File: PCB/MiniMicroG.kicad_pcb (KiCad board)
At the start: 2 copper layers, 111.9 x 88.1 mm, 21 parts, among them J1 .91"OLED, SW1 CHERRY_MX, SW2 CHERRY_MX, SW4 CHERRY_MX, SW5 CHERRY_MX, SW6 CHERRY_MX, SW7 RotaryEncoder_Switch, SW8 CHERRY_MX, U1 XIAO-RP2040-DIP

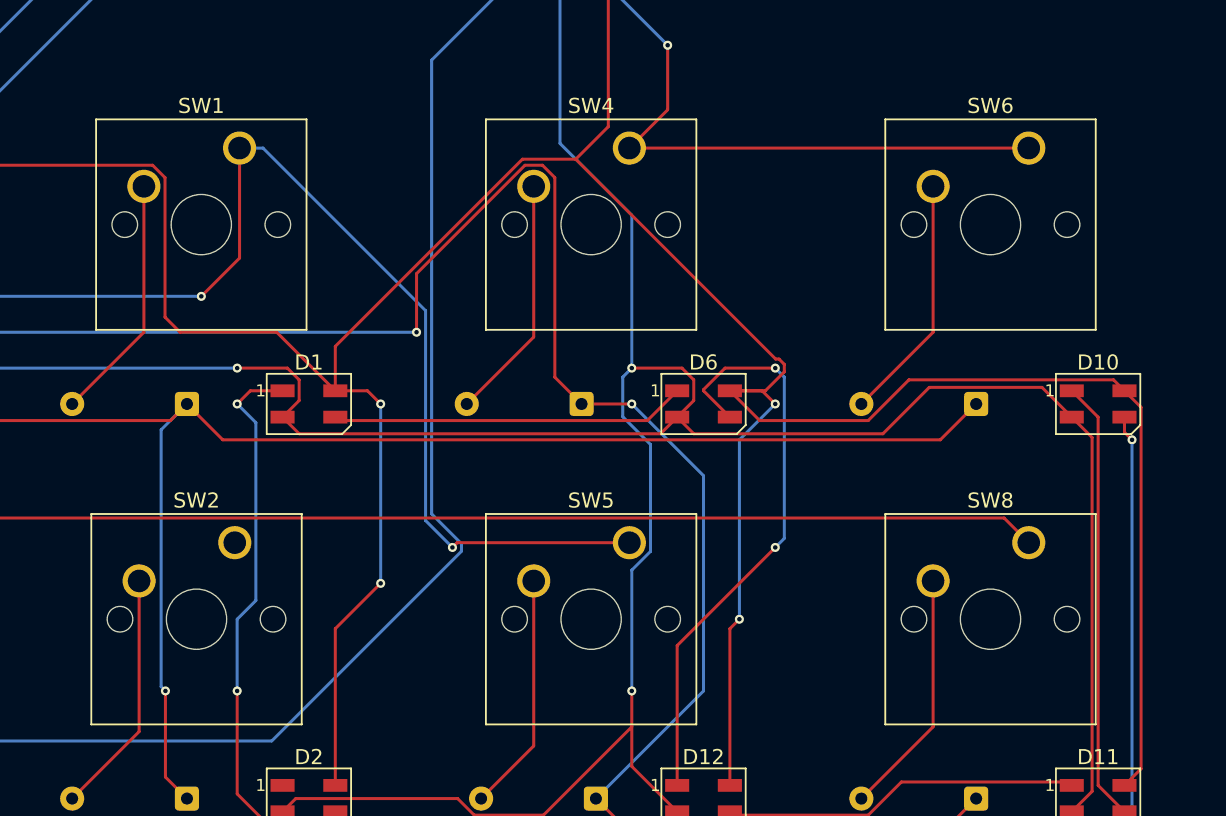
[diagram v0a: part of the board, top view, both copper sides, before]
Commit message: Add 3D Models
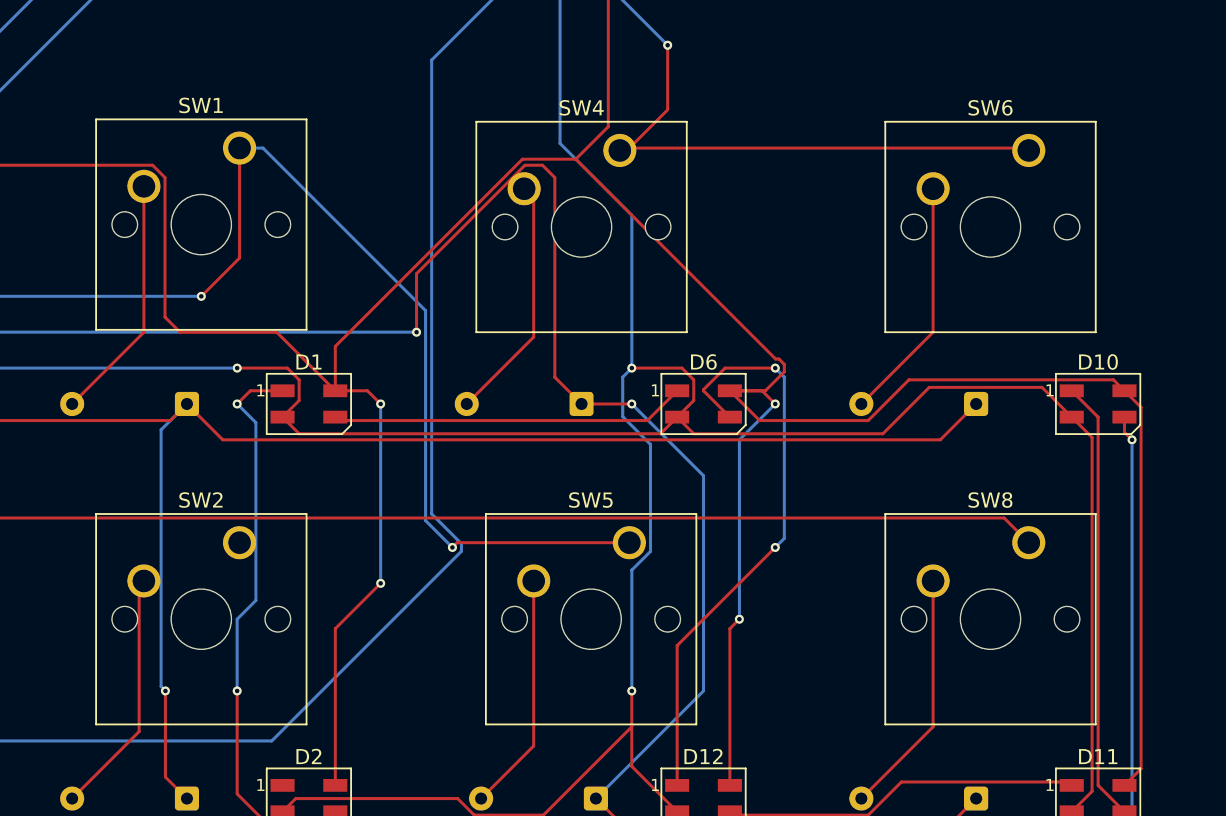
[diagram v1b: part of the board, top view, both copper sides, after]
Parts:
- moved SW4 0.65 mm to (149.2, 78.4)
- moved SW2 0.32 mm to (124.0, 104.5)
- moved SW6 0.16 mm to (176.4, 78.4)
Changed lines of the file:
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@@
 			)
 		)
+		(model "${KIPRJMOD}/3D Models/EVQV9_RotaryEncoder.step"
+			(offset
+				(xyz 7.5 -2 0)
+			)
+			(scale
+				(xyz 1 1 1)
+			)
+			(rotate
+				(xyz -0 -0 90)
+			)
+		)
 	)
 	(footprint "LED_SMD:LED_SK6812MINI_PLCC4_3.5x3.5mm_P1.75mm"
@@
 			)
 		)
+		(model "${KIPRJMOD}/3D Models/LED_SK6812MINI-E.step"
+			(offset
+				(xyz 0 5 -1)
+			)
+			(scale
+				(xyz 1 1 1)
+			)
+			(rotate
+				(xyz -0 -180 -0)
+			)
+		)
 	)
 	(footprint "Button_Switch_Keyboard:SW_Cherry_MX_1.00u_PCB"
@@
 			)
 		)
+		(model "${KIPRJMOD}/3D Models/cherry-mx-1.snapshot.3/asm_mx_asm_PCB.stp"
+			(offset
+				(xyz -2 -5 4)
+			)
+			(scale
+				(xyz 1 1 1)
+			)
+			(rotate
+				(xyz -0 -180 -90)
+			)
+		)
 	)
 	(footprint "Button_Switch_Keyboard:SW_Cherry_MX_1.00u_PCB"
@@
 		(model "${KICAD9_3DMODEL_DIR}/Button_Switch_Keyboard.3dshapes/SW_Cherry_MX_1.00u_PCB.step"
 			(offset
-				(xyz 0 0 0)
+				(xyz 2.1 0 0)
 			)
 			(scale
@@
 			)
 			(rotate
-				(xyz 0 0 0)
+				(xyz -0 -0 -0)
+			)
+		)
+		(model "${KIPRJMOD}/3D Models/cherry-mx-1.snapshot.3/asm_mx_asm_PCB.stp"
+			(offset
+				(xyz -2 -5 4)
+			)
+			(scale
+				(xyz 1 1 1)
+			)
+			(rotate
+				(xyz -0 -180 -90)
 			)
 		)
@@
 			)
 		)
+		(model "${KIPRJMOD}/3D Models/LED_SK6812MINI-E.step"
+			(offset
+				(xyz 0 5 -1)
+			)
+			(scale
+				(xyz 1 1 1)
+			)
+			(rotate
+				(xyz -0 -180 -0)
+			)
+		)
 	)
 	(footprint "LED_SMD:LED_SK6812MINI_PLCC4_3.5x3.5mm_P1.75mm"
@@
 			)
 		)
+		(model "${KIPRJMOD}/3D Models/LED_SK6812MINI-E.step"
+			(offset
+				(xyz 0 5 -1)
+			)
+			(scale
+				(xyz 1 1 1)
+			)
+			(rotate
+				(xyz -0 -180 -0)
+			)
+		)
 	)
 	(footprint "Seeed Studio XIAO Series Library:XIAO-RP2040-DIP"
@@
 			)
 		)
+		(model "${KIPRJMOD}/3D Models/Seeed Studio XIAO RP2040 v26.step"
+			(offset
+				(xyz 0 0 0)
+			)
+			(scale
+				(xyz 1 1 1)
+			)
+			(rotate
+				(xyz 0 0 0)
+			)
+		)
 	)
 	(footprint "Button_Switch_Keyboard:SW_Cherry_MX_1.00u_PCB"
 		(layer "F.Cu")
-		(at 123.66625 104.4575)
+		(at 123.98375 104.4575)
 		(descr "Cherry MX keyswitch, 1.00u, PCB mount, http://cherryamericas.com/wp-content/uploads/2014/12/mx_cat.pdf")
 		(tags "Cherry MX keyswitch 1.00u PCB")
@@
 			)
 		)
+		(model "${KIPRJMOD}/3D Models/cherry-mx-1.snapshot.3/asm_mx_asm_PCB.stp"
+			(offset
+				(xyz -2 -5 4)
+			)
+			(scale
+				(xyz 1 1 1)
+			)
+			(rotate
+				(xyz -0 -180 -90)
+			)
+		)
 	)
 	(footprint "KiCad-4_pin-SSD1306_OLED-.91-128x32:SSD1306-0.91-OLED-4pin-128x32"
@@
 		)
 		(embedded_fonts no)
+		(model "${KIPRJMOD}/3D Models/OLED_0.91_128x32.stp"
+			(offset
+				(xyz 19 -6 0)
+			)
+			(scale
+				(xyz 1 1 1)
+			)
+			(rotate
+				(xyz -0 -0 -180)
+			)
+		)
 	)
 	(footprint "LED_SMD:LED_SK6812MINI_PLCC4_3.5x3.5mm_P1.75mm"
@@
 			)
 		)
+		(model "${KIPRJMOD}/3D Models/LED_SK6812MINI-E.step"
+			(offset
+				(xyz 0 5 -1)
+			)
+			(scale
+				(xyz 1 1 1)
+			)
+			(rotate
+				(xyz -0 -180 -0)
+			)
+		)
 	)
 	(footprint "LED_SMD:LED_SK6812MINI_PLCC4_3.5x3.5mm_P1.75mm"
@@
 			)
 		)
+		(model "${KIPRJMOD}/3D Models/LED_SK6812MINI-E.step"
+			(offset
+				(xyz 0 5 -1)
+			)
+			(scale
+				(xyz 1 1 1)
+			)
+			(rotate
+				(xyz -0 -180 -0)
+			)
+		)
 	)
 	(footprint "Button_Switch_Keyboard:SW_Cherry_MX_1.00u_PCB"
 		(layer "F.Cu")
-		(at 149.86 78.26375)
+		(at 149.225 78.4225)
 		(descr "Cherry MX keyswitch, 1.00u, PCB mount, http://cherryamericas.com/wp-content/uploads/2014/12/mx_cat.pdf")
 		(tags "Cherry MX keyswitch 1.00u PCB")
@@
 			)
 		)
+		(model "${KIPRJMOD}/3D Models/cherry-mx-1.snapshot.3/asm_mx_asm_PCB.stp"
+			(offset
+				(xyz -2 -5 5)
+			)
+			(scale
+				(xyz 1 1 1)
+			)
+			(rotate
+				(xyz -0 180 -90)
+			)
+		)
 	)
 	(footprint "LED_SMD:LED_SK6812MINI_PLCC4_3.5x3.5mm_P1.75mm"
@@
 			)
 		)
+		(model "${KIPRJMOD}/3D Models/LED_SK6812MINI-E.step"
+			(offset
+				(xyz 0 5 -1)
+			)
+			(scale
+				(xyz 1 1 1)
+			)
+			(rotate
+				(xyz -0 -180 -0)
+			)
+		)
 	)
 	(footprint "Button_Switch_Keyboard:SW_Cherry_MX_1.00u_PCB"
@@
 			)
 		)
+		(model "${KIPRJMOD}/3D Models/cherry-mx-1.snapshot.3/asm_mx_asm_PCB.stp"
+			(offset
+				(xyz -2 -5 4)
+			)
+			(scale
+				(xyz 1 1 1)
+			)
+			(rotate
+				(xyz -0 -180 -90)
+			)
+		)
 	)
 	(footprint "Button_Switch_Keyboard:SW_Cherry_MX_1.00u_PCB"
 		(layer "F.Cu")
-		(at 176.37125 78.26375)
+		(at 176.37125 78.4225)
 		(descr "Cherry MX keyswitch, 1.00u, PCB mount, http://cherryamericas.com/wp-content/uploads/2014/12/mx_cat.pdf")
 		(tags "Cherry MX keyswitch 1.00u PCB")
@@
 		(embedded_fonts no)
 		(model "${KICAD9_3DMODEL_DIR}/Button_Switch_Keyboard.3dshapes/SW_Cherry_MX_1.00u_PCB.step"
+			(hide yes)
 			(offset
 				(xyz 0 0 0)
@@
 			)
 		)
+		(model "${KIPRJMOD}/3D Models/asm_mx.asm.16"
+			(hide yes)
+			(offset
+				(xyz 0 0 0)
+			)
+			(scale
+				(xyz 1 1 1)
+			)
+			(rotate
+				(xyz 0 0 0)
+			)
+		)
+		(model "${KIPRJMOD}/3D Models/cherry-mx-1.snapshot.3/asm_mx_asm_PCB.stp"
+			(offset
+				(xyz -2.5 -5 5)
+			)
+			(scale
+				(xyz 1 1 1)
+			)
+			(rotate
+				(xyz -0 -180 -90)
+			)
+		)
+		(model "${KIPRJMOD}/3D Models/cherry-mx-1.snapshot.3/asm_mx_asm_PLATE.stp"
+			(hide yes)
+			(offset
+				(xyz 2 0 0)
+			)
+			(scale
+				(xyz 1 1 1)
+			)
+			(rotate
+				(xyz -0 -0 -0)
+			)
+		)
 	)
 	(footprint "Diode_THT:D_DO-35_SOD27_P7.62mm_Horizontal"
@@
 		(width 0.2)
 		(layer "B.Cu")
-		(net 26)
-	)
-	(segment
-		(start 183.226 97.63125)
-		(end 183.35625 97.63125)
-		(width 0.2)
-		(layer "B.Cu")

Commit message: Update PCB
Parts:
- moved D9 25.3 mm to (149.0, 113.0), turned to 90 degrees
- moved D3 23.9 mm to (149.0, 94.8), turned to 90 degrees
- moved D10 23.4 mm to (158.0, 99.5)
- moved D11 23.1 mm to (158.0, 119.0), turned to 180 degrees
- moved D8 19.6 mm to (130.0, 113.0), turned to 90 degrees
- moved J1 18.5 mm to (168.9, 75.9)
- moved SW6 17.1 mm to (160.7, 85.1)
- moved D7 16.7 mm to (130.0, 95.0), turned to 90 degrees
- moved D6 16.4 mm to (139.0, 99.5)
- moved D12 15.7 mm to (139.2, 119.0), turned to 180 degrees
- moved SW8 15.7 mm to (160.7, 104.1)
- moved D5 13.5 mm to (110.0, 113.0), turned to 90 degrees
- moved SW7 10.6 mm to (108.0, 65.0)
- moved D4 10.5 mm to (110.0, 95.0), turned to 90 degrees
- moved D1 10.3 mm to (119.2, 99.5)
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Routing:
- net GND: track 267.0 -> 31.1 mm, vias 4 -> 7
- net +5V: track 252.8 -> 184.7 mm, vias 4 -> 0
- net Net-(U1-GPIO28/ADC2/A2): track 0.00 -> 63.6 mm
- net Net-(U1-GPIO27/ADC1/A1): track 0.00 -> 58.3 mm
- net Net-(D7-K): track 140.4 -> 82.2 mm
- net Net-(D3-K): track 114.6 -> 65.1 mm, vias 1 -> 0
- net Net-(D10-DIN): track 131.9 -> 105.0 mm, vias 1 -> 0
- net Net-(U1-GPIO1/RX): track 89.2 -> 63.3 mm, vias 3 -> 0
- net Net-(U1-GPIO0/TX): track 133.1 -> 108.4 mm, vias 1 -> 0
- net Net-(J1-Pin_3): track 124.6 -> 102.2 mm
- net Net-(U1-GPIO29/ADC3/A3): track 91.3 -> 109.9 mm, vias 1 -> 0
- net Net-(J1-Pin_4): track 105.5 -> 87.8 mm
- net Net-(D1-DOUT): track 37.9 -> 23.2 mm, vias 2 -> 0
- net Net-(U1-GPIO2/SCK): track 81.2 -> 69.3 mm
- net Net-(D3-A): track 16.4 -> 5.49 mm
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- added copper zone on B.Cu, net GND
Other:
- board size 111.9 x 88.1 mm -> 98 x 75 mm

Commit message: Update PCB
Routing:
- net GND: track 31.1 -> 70.7 mm
- net Net-(U1-GPIO29/ADC3/A3): track 109.9 -> 89.7 mm, vias 0 -> 3
- net Net-(D3-K): track 65.1 -> 84.1 mm
- net Net-(U1-GPIO28/ADC2/A2): track 63.6 -> 68.7 mm, vias 0 -> 2
- net +5V: track 184.7 -> 186.9 mm, vias 0 -> 2
- net Net-(J1-Pin_3): track 102.2 -> 103.1 mm

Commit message: Made the Casing
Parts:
- moved J1 3.16 mm to (167.9, 72.9)
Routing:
- net Net-(J1-Pin_3): track 103.1 -> 96.9 mm
- net +5V: track 186.9 -> 189.8 mm
- net Net-(J1-Pin_4): track 87.8 -> 88.0 mm, vias 0 -> 1
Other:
- board text added: "SCL"
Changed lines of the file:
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@@
 		(embedded_fonts no)
 		(model "${KICAD9_3DMODEL_DIR}/Rotary_Encoder.3dshapes/RotaryEncoder_Alps_EC11E-Switch_Vertical_H20mm.step"
+			(hide yes)
 			(offset
 				(xyz 0 0 0)
@@
 		)
 		(model "${KIPRJMOD}/3D Models/EVQV9_RotaryEncoder.step"
+			(hide yes)
 			(offset
 				(xyz 7.5 -2 0)
@@
 			)
 		)
+		(model "${KIPRJMOD}/3D Models/ec11.STEP"
+			(offset
+				(xyz 7.5 -2.5 0)
+			)
+			(scale
+				(xyz 1 1 1)
+			)
+			(rotate
+				(xyz -90 -0 -90)
+			)
+		)
+		(model "${KIPRJMOD}/3D Models/EC11-THT-15F-black.step"
+			(hide yes)
+			(offset
+				(xyz 7.5 -2.5 0)
+			)
+			(scale
+				(xyz 1 1 1)
+			)
+			(rotate
+				(xyz -0 -0 90)
+			)
+		)
 	)
 	(footprint "LED_SMD:LED_SK6812MINI_PLCC4_3.5x3.5mm_P1.75mm"
@@
 	(footprint "KiCad-4_pin-SSD1306_OLED-.91-128x32:SSD1306-0.91-OLED-4pin-128x32"
 		(layer "F.Cu")
-		(at 168.885 75.885 180)
+		(at 167.885 72.885 180)
 		(property "Reference" "J1"
 			(at 1.9 5.91 90)
@@
 			)
 		)
-		(fp_text user "SCL"
-			(at 34.5 7.27 90)
-			(layer "F.SilkS")
-			(effects
-				(font
-					(size 0.75 0.75)
-					(thickness 0.15)
-				)
-			)
-		)
 		(pad "1" thru_hole rect
 			(at 36.5 2.19 180)
@@
 		)
 	)
+	(gr_text "SCL"
+		(at 133.385 65.615 90)
+		(layer "F.SilkS")
+		(effects
+			(font
+				(size 0.75 0.75)
+				(thickness 0.15)
+			)
+		)
+	)
 	(gr_text "Created by @codecooker1"
 		(at 104 55 -0)
@@
 	)
 	(segment
-		(start 135 80.538274)
-		(end 135 72.885)
-		(width 0.3)
-		(layer "F.Cu")
-		(net 3)
-	)
-	(segment
 		(start 137.5 119.875)
 		(end 136.724 120.651)
@@
 	)
 	(segment
-		(start 143.546 86.546)
-		(end 141.007726 86.546)
-		(width 0.3)
-		(layer "F.Cu")
-		(net 3)
-	)
-	(segment
 		(start 120.224 97.899)
 		(end 111.101 97.899)
@@
 	)
 	(segment
-		(start 133.27 71.155)
-		(end 132.385 71.155)
-		(width 0.3)
-		(layer "F.Cu")
-		(net 3)
-	)
-	(segment
 		(start 136.724 120.651)
 		(end 118.276 120.651)
@@
 	)
 	(segment
-		(start 141.007726 86.546)
-		(end 135 80.538274)
-		(width 0.3)
-		(layer "F.Cu")
-		(net 3)
-	)
-	(segment
 		(start 158.974 97.899)
 		(end 159.75 98.675)
@@
 	)
 	(segment
+		(start 135 80.538274)
+		(end 135 71.77)
+		(width 0.3)
+		(layer "F.Cu")
+		(net 3)
+	)
+	(segment
 		(start 152 97.899)
 		(end 158.974 97.899)
@@
 	)
 	(segment
+		(start 152 97.899)
+		(end 152 95)
+		(width 0.3)
+		(layer "F.Cu")
+		(net 3)
+	)
+	(segment
 		(start 156.25 119.875)
 		(end 155.474 120.651)
@@
 	)
 	(segment
-		(start 152 95)
-		(end 143.546 86.546)
+		(start 135 71.77)
+		(end 131.385 68.155)
 		(width 0.3)
 		(layer "F.Cu")
@@
 	)
 	(segment
-		(start 152 97.899)
-		(end 152 95)
+		(start 106.349 97.651)
+		(end 85.53137 97.651)
 		(width 0.3)
 		(layer "F.Cu")
@@
 	)
 	(segment
-		(start 106.349 97.651)
-		(end 85.53137 97.651)
+		(start 108 96)
+		(end 106.349 97.651)
 		(width 0.3)
 		(layer "F.Cu")
@@
 	)
 	(segment
-		(start 108 96)
-		(end 106.349 97.651)
+		(start 143.546 86.546)
+		(end 141.007726 86.546)
 		(width 0.3)
 		(layer "F.Cu")
@@
 	)
 	(segment
-		(start 135 72.885)
-		(end 133.27 71.155)
+		(start 152 95)
+		(end 143.546 86.546)
+		(width 0.3)
+		(layer "F.Cu")
+		(net 3)
+	)
+	(segment
+		(start 141.007726 86.546)
+		(end 135 80.538274)
 		(width 0.3)
 		(layer "F.Cu")
@@
 	)
 	(segment
+		(start 126.649 66.351)
+		(end 127 66)
+		(width 0.3)
+		(layer "F.Cu")
+		(net 6)
+	)
+	(segment
 		(start 114.684662 66.351)
-		(end 132.109 66.351)
+		(end 126.649 66.351)
 		(width 0.3)
 		(layer "F.Cu")
@@
 	)
 	(segment
-		(start 132.109 66.351)
-		(end 132.385 66.075)
+		(start 92.04 117.62)
+		(end 80.767 106.347)
 		(width 0.3)
 		(layer "F.Cu")
 		(net 6)
 	)
+	(via
+		(at 127 66)
+		(size 0.6)
+		(drill 0.3)
+		(layers "F.Cu" "B.Cu")
+		(net 6)
+	)
 	(segment
-		(start 92.04 117.62)
-		(end 80.767 106.347)
+		(start 127 66)
+		(end 128.46 66)
 		(width 0.3)
-		(layer "F.Cu")
+		(layer "B.Cu")
 		(net 6)
 	)
 	(segment
-		(start 116.678141 63.649)
-		(end 132.653236 63.649)
+		(start 128.46 66)
+		(end 131.385 63.075)
 		(width 0.3)
-		(layer "F.Cu")
-		(net 7)
+		(layer "B.Cu")
+		(net 6)
 	)
 	(segment
@@
 	)
 	(segment
+		(start 116.66357 63.66357)
+		(end 116.678141 63.649)
+		(width 0.3)
+		(layer "F.Cu")
+		(net 7)
+	)
+	(segment
 		(start 90.927 119.731338)
 		(end 90.927 117.21552)
@@
 	(segment
 		(start 80.266 100.061141)
-		(end 116.678141 63.649)
+		(end 116.66357 63.66357)
 		(width 0.3)
 		(layer "F.Cu")
@@
 	)
 	(segment
-		(start 134 67)
-		(end 132.385 68.615)
+		(start 116.66357 63.66357)
+		(end 117.07614 63.251)
 		(width 0.3)
 		(layer "F.Cu")
@@
 	)
 	(segment
-		(start 134 64.995764)
-		(end 134 67)
+		(start 129.021 63.251)
+		(end 131.385 65.615)
 		(width 0.3)
 		(layer "F.Cu")
@@
 	)
 	(segment
-		(start 132.653236 63.649)
-		(end 134 64.995764)
+		(start 117.07614 63.251)
+		(end 129.021 63.251)
 		(width 0.3)
 		(layer "F.Cu")

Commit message: Update PCB
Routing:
- net GND: track 70.7 -> 24.2 mm
- net Net-(U1-GPIO2/SCK): track 69.3 -> 77.5 mm
- net Net-(U1-GPIO1/RX): track 63.3 -> 65.3 mm, vias 0 -> 1
- net +5V: track 189.8 -> 188.4 mm
- net Net-(D7-K): track 82.2 -> 83.0 mm
